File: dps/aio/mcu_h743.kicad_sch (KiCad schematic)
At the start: 0 parts

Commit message: feat: draw the clear part of the H743 core, document the AIO, and explain it on an interactive page
- mcu_h743: STM32H743VIH6 (TFBGA-100) with supply and decoupling per ST
  AN4938 (100 nF per VDD + 4.7 uF, VDDLDO 4.7 uF, VCAP1+VCAP2 joined with
  2x 2.2 uF, VDDA and VDD33USB 100 nF + 1 uF, VBAT 100 nF), BOOT0 and
  PDR_ON, SWD/DFU pads, USB-C from OpenAIO, battery divider 100k/10k and
  I2C2 pull-ups; every pin labelled per the MicoAir743v2 hwdef. Crystal,
  baro, logging, second IMU and peripheral connectors stay open.
- IMU INT2 (OpenAIO's CLKIN) left unconnected, as on the MicoAir; +5V_USB
  joins the power sheet; ERC is down to 17 errors, all explained.
- NAVRH.md: every sheet and block with its source and reason, the power
  tree, connectors, ArduPilot settings and open questions; tabulky.py
  regenerates its pin map, cross-sheet nets and BOM from the netlist.
- web/: build.py turns the schematic into one page with clickable blocks
  (what, why, where from), texts in obsah.py; the 5 MB output is ignored.

Co-Authored-By: Claude Opus 5.5 <noreply@anthropic.com>
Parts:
- added C301, C302, C303, C308, C310, C312, C313, C314: 100n, lib:C_0201_0603Metric, symbol lib:C
- added C304, C305: 4.7uF, lib:C_0402_1005Metric, symbol lib:C
- added C306, C307: 2.2uF, lib:C_0402_1005Metric, symbol lib:C
- added C309, C311: 1uF, lib:C_0402_1005Metric, symbol lib:C
- added J301: TYPE-C 16P QTWT, lib:USB-TYPE-C-SMD_TYPE-C-16P-QTWT, symbol lib:TYPE-C16PQTWT
- added R301, R302, R304: 10k, lib:R_0201_0603Metric, symbol lib:R
- added R303: 100k, lib:R_0201_0603Metric, symbol lib:R
- added R305, R306: 2.2k, lib:R_0201_0603Metric, symbol lib:R
- added R307, R308: 5.1k, lib:R_0201_0603Metric, symbol lib:R
- added TP301: BOOT0, lib:TestPoint_Pad_D1.0mm, symbol lib:TestPoint
- added TP302: +3.3V, lib:TestPoint_Pad_D1.0mm, symbol lib:TestPoint
- added TP303: SWDIO, lib:TestPoint_Pad_D1.0mm, symbol lib:TestPoint
- added TP304: SWCLK, lib:TestPoint_Pad_D1.0mm, symbol lib:TestPoint
- added TP305: NRST, lib:TestPoint_Pad_D1.0mm, symbol lib:TestPoint
- added TP306: GND, lib:TestPoint_Pad_D1.0mm, symbol lib:TestPoint
- added U301: STM32H743VIH6, Package_BGA:TFBGA-100_8x8mm_Layout10x10_P0.8mm, symbol MCU_ST_STM32H7:STM32H743VIHx
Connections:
- net ESC_CURRENT: now also U301.F2 (PC1)
- net IMU_CS: now also U301.A8 (PA15)
- net IMU_INT: now also U301.A5 (PB7)
- net LIDAR_PWM: now also U301.J4 (PB0)
- net LIDAR_TX: now also U301.C5 (PB5)
- net MOTOR1: now also U301.G7 (PE14)
- net MOTOR2: now also U301.K6 (PE13)
- net MOTOR3: now also U301.H6 (PE11)
- net MOTOR4: now also U301.K5 (PE9)
- net RC_RX: now also U301.E10 (PC7)
- net SCL: now also R306.2, U301.J7 (PB10)
- net SDA: now also R305.2, U301.K7 (PB11)
- net VTX_EN: now also U301.J10 (PD13)
- net VTX_RX: now also U301.K2 (PA3)
- net VTX_TX: now also U301.J2 (PA2)
- new net +3.3V: C301.1, C302.1, C303.1, C304.1, C305.1, C308.1, C309.1, C310.1, C311.1, C312.1, R301.1, R305.1, R306.1, TP302.1, U301.B2 (VBAT), U301.D2 (VDD), U301.F4 (VDDLDO), U301.F5 (VDD), U301.F6 (VDD33_USB), U301.H1 (VDDA), U301.K1 (VDD)
- new net +5V_USB: J301.A4 (VBUS), J301.A9 (VBUS)
- new net +BATT: R303.1
- new net BOOT0: R302.1, TP301.1, U301.D5 (BOOT0)
- new net BUZZER: U301.G8 (PD15)
- new net EXT_SCL: U301.B4 (PB8)
- new net EXT_SDA: U301.A4 (PB9)
- new net FLOW_RX: U301.H2 (PA1)
- new net FLOW_TX: U301.G2 (PA0)
- new net GND: C301.2, C302.2, C303.2, C304.2, C305.2, C306.2, C307.2, C308.2, C309.2, C310.2, C311.2, C312.2, C313.2, C314.2, J301.0 (EH), J301.A1 (GND), J301.A12 (GND), R302.2, R304.2, R307.2, R308.2, TP306.1, U301.C2 (VSS), U301.E4 (VSS), U301.E5 (VSS), U301.E6 (VSS), U301.G1 (VSSA), U301.J1 (VSS)
- new net GPS_RX: U301.J9 (PD9)
- new net GPS_TX: U301.K9 (PD8)
- new net HSE_IN: U301.C1 (PH0)
- new net HSE_OUT: U301.D1 (PH1)
- new net IMU2_ACC_CS: U301.D7 (PD4)
- new net IMU2_ACC_INT: U301.A1 (PC14)
- new net IMU2_GYR_CS: U301.B6 (PD5)
- new net IMU2_GYR_INT: U301.B1 (PC15)
- new net IMU2_MISO: U301.E2 (PC2_C)
- new net IMU2_MOSI: U301.F3 (PC3_C)
- new net IMU2_SCK: U301.C7 (PD3)
- new net IMU_SPI.MISO: U301.A6 (PB4)
- new net IMU_SPI.MOSI: U301.C6 (PD6)
- new net IMU_SPI.SCK: U301.A7 (PB3)
- new net LED_B: U301.C3 (PE4)
- new net LED_G: U301.A3 (PE2)
- new net LED_R: U301.B3 (PE3)
- new net NRST: C313.1, TP305.1, U301.E1 (NRST)
- new net PDR_ON: R301.2, U301.F7 (PDR_ON)
- new net PWM10: U301.E3 (PE6)
- new net PWM11: U301.H8 (PD14)
- new net PWM5: U301.K4 (PB1)
- new net PWM7: U301.K10 (PD12)
- new net PWM9: U301.D3 (PE5)
- new net RC_TX: U301.F10 (PC6)
- new net SD_CK: U301.C8 (PC12)
- new net SD_CMD: U301.B7 (PD2)
- new net SD_D0: U301.F9 (PC8)
- new net SD_D1: U301.E9 (PC9)
- new net SD_D2: U301.B9 (PC10)
- new net SD_D3: U301.B8 (PC11)
- new net SWCLK: TP304.1, U301.A9 (PA14)
- new net SWDIO: TP303.1, U301.A10 (PA13)
- new net UART1_RX: U301.D10 (PA10)
- new net UART1_TX: U301.C9 (PA9)
- new net UART5_TX: U301.B5 (PB6)
- new net UART7_RX: U301.H5 (PE7)
- new net UART7_TX: U301.J5 (PE8)
- new net UART8_RX: U301.D4 (PE0)
- new net UART8_TX: U301.C4 (PE1)
- new net USB_CC1: J301.A5 (CC1), R307.1
- new net USB_CC2: J301.B5 (CC2), R308.1
- new net USB_DM: J301.A7 (DN1), J301.B7 (DN2), U301.C10 (PA11)
- new net USB_DP: J301.A6 (DP1), J301.B6 (DP2), U301.B10 (PA12)
- new net VBAT_SENSE: C314.1, R303.2, R304.1, U301.F1 (PC0)
- new net VCAP: C306.1, C307.1, U301.E7 (VCAP), U301.F8 (VCAP)
- no-connect marks 0 -> 23
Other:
- note added: "MCU STM32H743VIH6 (TFBGA-100), jako MicoAir. Piny podle hwdef MicoAir743v2, kuličky podle symbolu KiCad. Napájení podle ST AN4938 kap. 2.2: 100 nF na každý VDD + 4,7 µF; VDDLDO 4,7 µF; VCAP1+VCAP2 spojené, 2× 2,2 µF; VDDA 100 nF + 1 µF; VDD33USB z VDD, 100 nF + 1 µF; VBAT na VDD + 100 nF; PDR_ON 10k na VDD; BOOT0 10k na GND. Plný popis a zdroje: dps/aio/NAVRH.md"
- note added: "NENAKRESLENO (rozhodne se ručně): - krystal 8 MHz na HSE_IN/HSE_OUT; kondenzátory podle CL krystalu [AN2867] - baro na SDA/SCL (MicoAir: SPL06 0x77 na I2C2 = bus 0) - logování: microSD na SD_* (SDMMC1) nebo SPI flash - druhá IMU BMI088 na IMU2_* (SPI2) ano/ne - konektory: GPS (GPS_*, EXT_SDA/SCL), MTF-02P (FLOW_*), XR1 Nano (RC_TX/RC_RX), Bluetooth (UART1 nebo UART8) - RGB LED na LED_R/G/B (aktiv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"
- note removed: "MCU STM32H743 — NENAKRESLENO, kreslí se ručně. Rozhrani k ostatním listům jsou hierarchické štítky vlevo a vpravo. Pinout podle hwdef MicoAir743v2 (external/ardupilot/libraries/AP_HAL_ChibiOS/hwdef/MicoAir743v2/hwdef.dat). Co sem patří (viz dps/docs/04_pozadavky.md, kap. 2.4–2.8): - STM32H743VIH6 (TFBGA-100), VCAP, blokování, krystal 8 MHz, BOOT0 tlačítko, SWD pady, reset [ST AN4938] - USB-C (USB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"
- title: MCU STM32H743 — k nakreslení -> MCU STM32H743

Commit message: feat: add the crystal, baro, BMI088 and microSD to the AIO's H743 sheet
- Y301 YXC X32258MOB4SI 8 MHz, CL 12 pF, with 15 pF load caps per
  AN4938/AN2867; gm_crit ~0.5 mA/V against the H743's 1.5 mA/V limit.
- U302: one LGA-8 footprint for SPL06-001 or DPS310 (same package, pins and
  addresses as the BMP280), I2C at 0x77. Both chips report ID 0x10, so the
  hwdef lists only SPL06; a DPS310 swaps that one line.
- U303 BMI088 on SPI2 as on MicoAir (PS low, SDO1+SDO2 on MISO, INT1/INT3 as
  data ready); J302 microSD from OpenAIO on SDMMC1 with 47k pull-ups.
- ERC: 18 errors, the new one the BMI088's joined SDO outputs, as its
  datasheet asks for SPI. NAVRH, README, hwdef README and the web texts
  follow; blocks may list parts placed elsewhere on the sheet.

Co-Authored-By: Claude Opus 5.5 <noreply@anthropic.com>
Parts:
- added C317, C318, C319, C320: 100n, lib:C_0201_0603Metric, symbol lib:C
- added C321: 4.7uF, lib:C_0402_1005Metric, symbol lib:C
- added C322, C323: 15pF C0G, lib:C_0402_1005Metric, symbol lib:C
- added J302: TF-021B-H265, lib:TF-SMD_TF-021B-H265, symbol lib:TF-021B-H265
- added R309, R310, R311, R312, R313: 47k, lib:R_0201_0603Metric, symbol lib:R
- added TP301: BOOT0, lib:TestPoint_Pad_D1.0mm, symbol lib:TestPoint
- added U302: SPL06-001 / DPS310, Package_LGA:Bosch_LGA-8_2x2.5mm_P0.65mm_ClockwisePinNumbering, symbol Sensor_Pressure:BMP280
- added U303: BMI088, Package_LGA:Bosch_LGA-16_4.5x3mm_P0.5mm_LayoutBorder7x1y_ClockwisePinNumbering, symbol Sensor_Motion:BMI088
- Y301: renamed from TP301; value BOOT0 -> 8MHz 12pF X32258MOB4SI; footprint lib:TestPoint_Pad_D1.0mm -> Crystal:Crystal_SMD_3225-4Pin_3.2x2.5mm; symbol lib:TestPoint -> Device:Crystal_GND24; LCSC (none) -> C2682775
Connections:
- net +3.3V: now also C317.1, C318.1, C319.1, C320.1, C321.1, J302.4 (VDD), R309.1, R310.1, R311.1, R312.1, R313.1, U302.2 (CSB), U302.5 (SDO), U302.6 (VDDIO), U302.8 (VDD), U303.11 (VDDIO), U303.3 (VDD)
- net BOOT0: now also TP301.1; no longer Y301.1
- net GND: now also Y301.2 (G), Y301.4 (G), C317.2, C318.2, C319.2, C320.2, C321.2, C322.2, C323.2, J302.10, J302.6 (VSS), J302.9, U302.1 (GND), U302.7 (GND), U303.2 (GNDA), U303.4 (GNDA), U303.6 (GNDIO), U303.7 (PS)
- net HSE_IN: now also Y301.1, C322.1
- net HSE_OUT: now also Y301.3, C323.1
- net IMU2_ACC_CS: now also U303.14 (~{CSB1})
- net IMU2_ACC_INT: now also U303.16 (INT1)
- net IMU2_GYR_CS: now also U303.5 (~{CSB2})
- net IMU2_GYR_INT: now also U303.12 (INT3)
- net IMU2_MISO: now also U303.10 (SDO2), U303.15 (SDO1)
- net IMU2_MOSI: now also U303.9 (SDI/SDA)
- net IMU2_SCK: now also U303.8 (SCK/SCL)
- net SCL: now also U302.4 (SCK)
- net SDA: now also U302.3 (SDI)
- net SD_CK: now also J302.5 (CLX)
- net SD_CMD: now also J302.3 (CMD), R309.2
- net SD_D0: now also J302.7 (DAT0), R310.2
- net SD_D1: now also J302.8 (DAT1), R311.2
- net SD_D2: now also J302.1 (DAT2), R312.2
- net SD_D3: now also J302.2 (CD/DAT3), R313.2
- no-connect marks 23 -> 25
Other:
- note added: "J302 microSD na SDMMC1, pull-upy 47k na CMD a D0–D3 (SD: 10–100k)."
- note added: "NENAKRESLENO (rozhodne se ručně): - konektory: GPS (GPS_*, EXT_SDA/SCL), MTF-02P (FLOW_*), XR1 Nano (RC_TX/RC_RX), Bluetooth (UART1 nebo UART8) - RGB LED na LED_R/G/B (aktivní v nule), bzučák na BUZZER - volné PWM5, 7, 9–11 na pady - obrys 36 × 36 mm, díry 26 × 26 (Pavo20)"
- note added: "U302: SPL06-001 a DPS310 mají stejné pouzdro i piny (jako BMP280). CSB a SDO na 3,3 V → I2C, adresa 0x77. Osadit podle skladu JLC."
- note added: "U303 BMI088 jako MicoAir: SPI2, PS = GND (SPI), SDO1+SDO2 = MISO, INT1 = data ready akcel., INT3 = gyro."
- note added: "Y301: CL 12 pF, C = 2 × (CL − Cstray) = 2 × (12 − 5) = 14 → 15 pF [AN4938, AN2867]. gm_crit = 4·ESR·(2πf)²·(C0+CL)² ≈ 0,5 mA/V (ESR 180 Ω, C0 ≤ 5 pF) < Gmcritmax 1,5 mA/V [DS12110]."
- note removed: "NENAKRESLENO (rozhodne se ručně): - krystal 8 MHz na HSE_IN/HSE_OUT; kondenzátory podle CL krystalu [AN2867] - baro na SDA/SCL (MicoAir: SPL06 0x77 na I2C2 = bus 0) - logování: microSD na SD_* (SDMMC1) nebo SPI flash - druhá IMU BMI088 na IMU2_* (SPI2) ano/ne - konektory: GPS (GPS_*, EXT_SDA/SCL), MTF-02P (FLOW_*), XR1 Nano (RC_TX/RC_RX), Bluetooth (UART1 nebo UART8) - RGB LED na LED_R/G/B (aktiv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"

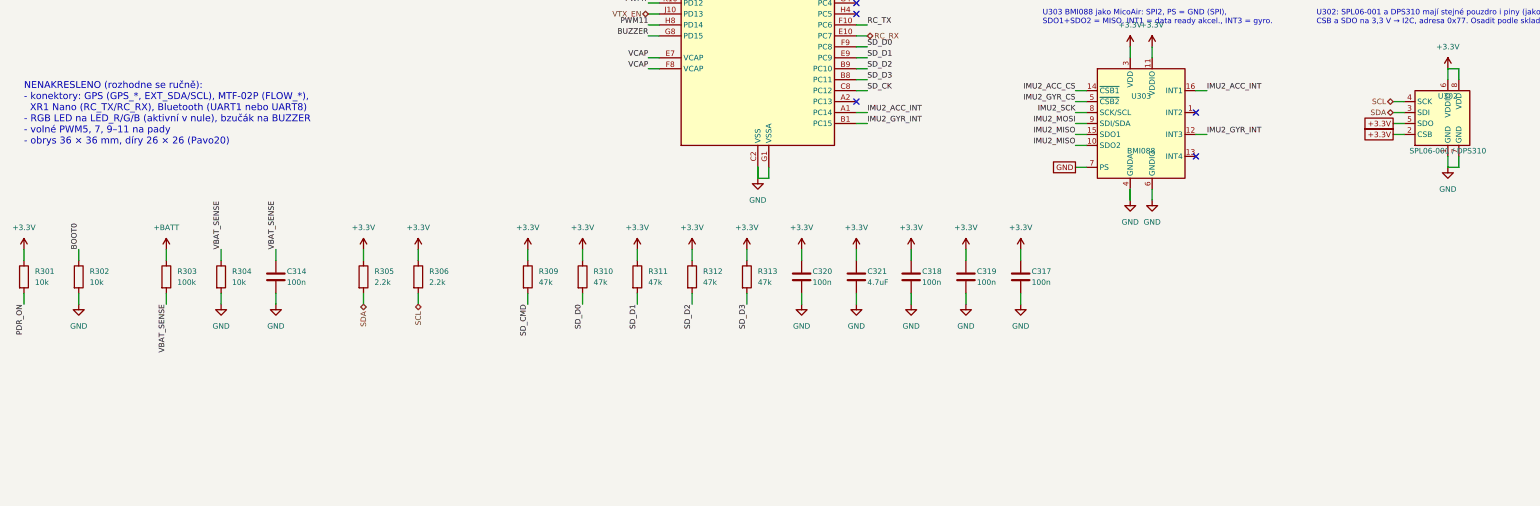
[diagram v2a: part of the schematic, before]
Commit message: feat: add the peripheral connectors to the AIO, from the makers' pinouts
- J303 SH1.0-6P for the WS-M181 GPS in the order printed on the module
  (TX RX GND 5V SCL SDA), with 4.7k pull-ups on the external I2C for its
  IST8310; J304 SH1.0-4P for the MTF-02P (GND 5V Rx Tx, robofusion; MicoAir
  draws the same signals from the other end). Neither maker says where pin 1
  is, so both are marked to check with a meter before first power.
- Pads for the XR1 Nano (it has castellated pads, no connector), UART1 and
  UART8, and the free PWM5, 7, 9, 10, 11.
- J201 pin 6 (SBUS from a DJI unit) now reaches USART6 RX only through JP202,
  open by default: the XR1's TX drives that line, and MicoAir's hard link
  would put two transmitters on it.
- NAVRH, README, hwdef comment and web texts follow; ERC still 18, explained.

Co-Authored-By: Claude Opus 5.5 <noreply@anthropic.com>
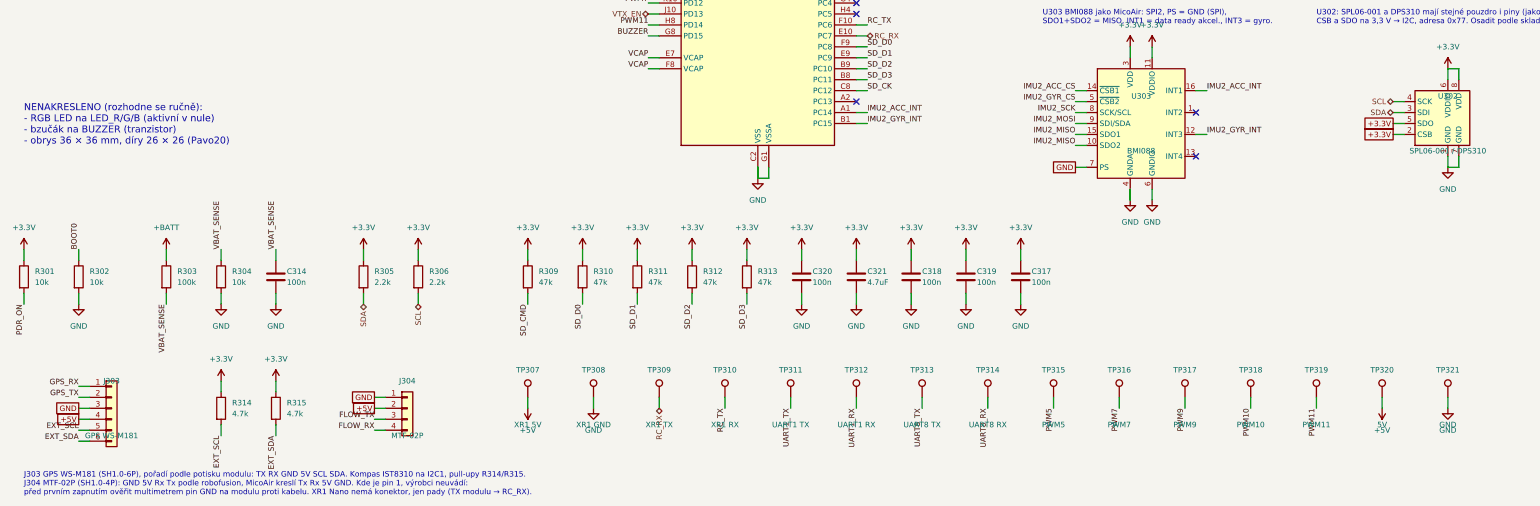
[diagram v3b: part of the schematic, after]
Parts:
- added J303: GPS WS-M181, Connector_JST:JST_SH_SM06B-SRSS-TB_1x06-1MP_P1.00mm_Horizontal, symbol Connector_Generic:Conn_01x06
- added J304: MTF-02P, Connector_JST:JST_SH_SM04B-SRSS-TB_1x04-1MP_P1.00mm_Horizontal, symbol Connector_Generic:Conn_01x04
- added R314, R315: 4.7k, lib:R_0201_0603Metric, symbol lib:R
- added TP307: XR1 5V, lib:TestPoint_Pad_D1.0mm, symbol lib:TestPoint
- added TP308: XR1 GND, lib:TestPoint_Pad_D1.0mm, symbol lib:TestPoint
- added TP309: XR1 TX, lib:TestPoint_Pad_D1.0mm, symbol lib:TestPoint
- added TP310: XR1 RX, lib:TestPoint_Pad_D1.0mm, symbol lib:TestPoint
- added TP311: UART1 TX, lib:TestPoint_Pad_D1.0mm, symbol lib:TestPoint
- added TP312: UART1 RX, lib:TestPoint_Pad_D1.0mm, symbol lib:TestPoint
- added TP313: UART8 TX, lib:TestPoint_Pad_D1.0mm, symbol lib:TestPoint
- added TP314: UART8 RX, lib:TestPoint_Pad_D1.0mm, symbol lib:TestPoint
- added TP315: PWM5, lib:TestPoint_Pad_D1.0mm, symbol lib:TestPoint
- added TP316: PWM7, lib:TestPoint_Pad_D1.0mm, symbol lib:TestPoint
- added TP317: PWM9, lib:TestPoint_Pad_D1.0mm, symbol lib:TestPoint
- added TP318: PWM10, lib:TestPoint_Pad_D1.0mm, symbol lib:TestPoint
- added TP319: PWM11, lib:TestPoint_Pad_D1.0mm, symbol lib:TestPoint
- added TP320: 5V, lib:TestPoint_Pad_D1.0mm, symbol lib:TestPoint
- added TP321: GND, lib:TestPoint_Pad_D1.0mm, symbol lib:TestPoint
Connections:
- net +3.3V: now also R314.1, R315.1
- net EXT_SCL: now also J303.5 (Pin_5), R314.2
- net EXT_SDA: now also J303.6 (Pin_6), R315.2
- net FLOW_RX: now also J304.4 (Pin_4)
- net FLOW_TX: now also J304.3 (Pin_3)
- net GND: now also J303.3 (Pin_3), J304.1 (Pin_1), TP308.1, TP321.1
- net GPS_RX: now also J303.1 (Pin_1)
- net GPS_TX: now also J303.2 (Pin_2)
- net PWM10: now also TP318.1
- net PWM11: now also TP319.1
- net PWM5: now also TP315.1
- net PWM7: now also TP316.1
- net PWM9: now also TP317.1
- net RC_RX: now also TP309.1
- net RC_TX: now also TP310.1
- net UART1_RX: now also TP312.1
- net UART1_TX: now also TP311.1
- net UART8_RX: now also TP314.1
- net UART8_TX: now also TP313.1
- new net +5V: J303.4 (Pin_4), J304.2 (Pin_2), TP307.1, TP320.1
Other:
- note added: "J303 GPS WS-M181 (SH1.0-6P), pořadí podle potisku modulu: TX RX GND 5V SCL SDA. Kompas IST8310 na I2C1, pull-upy R314/R315. J304 MTF-02P (SH1.0-4P): GND 5V Rx Tx podle robofusion, MicoAir kreslí Tx Rx 5V GND. Kde je pin 1, výrobci neuvádí: před prvním zapnutím ověřit multimetrem pin GND na modulu proti kabelu. XR1 Nano nemá konektor, jen pady (TX modulu → RC_RX)."
- note added: "NENAKRESLENO (rozhodne se ručně): - RGB LED na LED_R/G/B (aktivní v nule) - bzučák na BUZZER (tranzistor) - obrys 36 × 36 mm, díry 26 × 26 (Pavo20)"
- note removed: "NENAKRESLENO (rozhodne se ručně): - konektory: GPS (GPS_*, EXT_SDA/SCL), MTF-02P (FLOW_*), XR1 Nano (RC_TX/RC_RX), Bluetooth (UART1 nebo UART8) - RGB LED na LED_R/G/B (aktivní v nule), bzučák na BUZZER - volné PWM5, 7, 9–11 na pady - obrys 36 × 36 mm, díry 26 × 26 (Pavo20)"
